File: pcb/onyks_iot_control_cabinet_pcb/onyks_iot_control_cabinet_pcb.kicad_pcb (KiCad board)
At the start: 2 copper layers, 70 x 82 mm, 45 parts, among them J1 Conn_02x05_Odd_Even, J2 Conn_01x06_Pin, J3 Screw_Terminal_01x02, J4 Jack-DC, J5 Conn_01x03_Pin, J6 Screw_Terminal_01x02, J7 Conn_01x02_Socket, J8 Conn_02x09_Odd_Even, J9 Conn_01x06_Socket, Q1 NPN, Q2 NPN, Q3 PMV100ENEAR, Q4 PMV100ENEAR, SW1 SW_Push, SW2 SW_Push, SW3 SW_Push, U1 ESP32-WROOM-32D, U2 LMR51430XDDCR

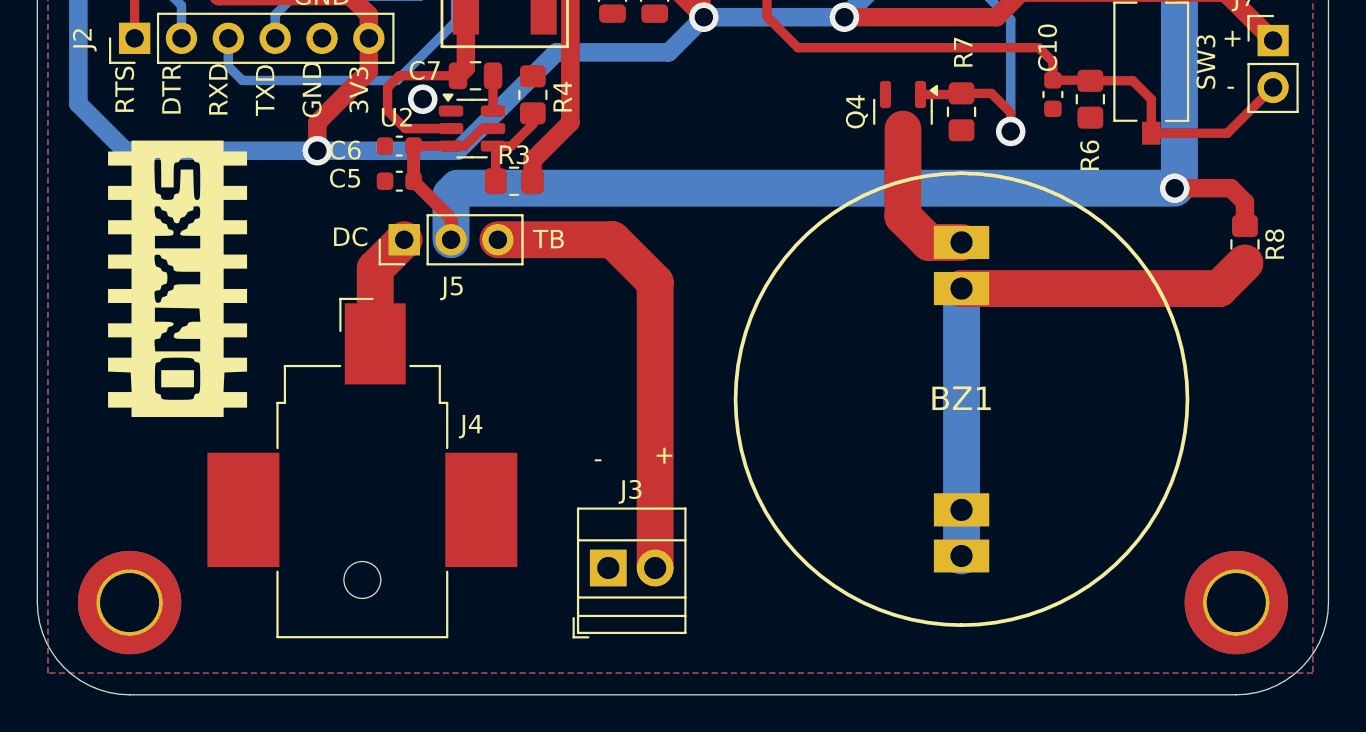
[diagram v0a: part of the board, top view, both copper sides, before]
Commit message: Update the PCB and schematics; add the potentiometer
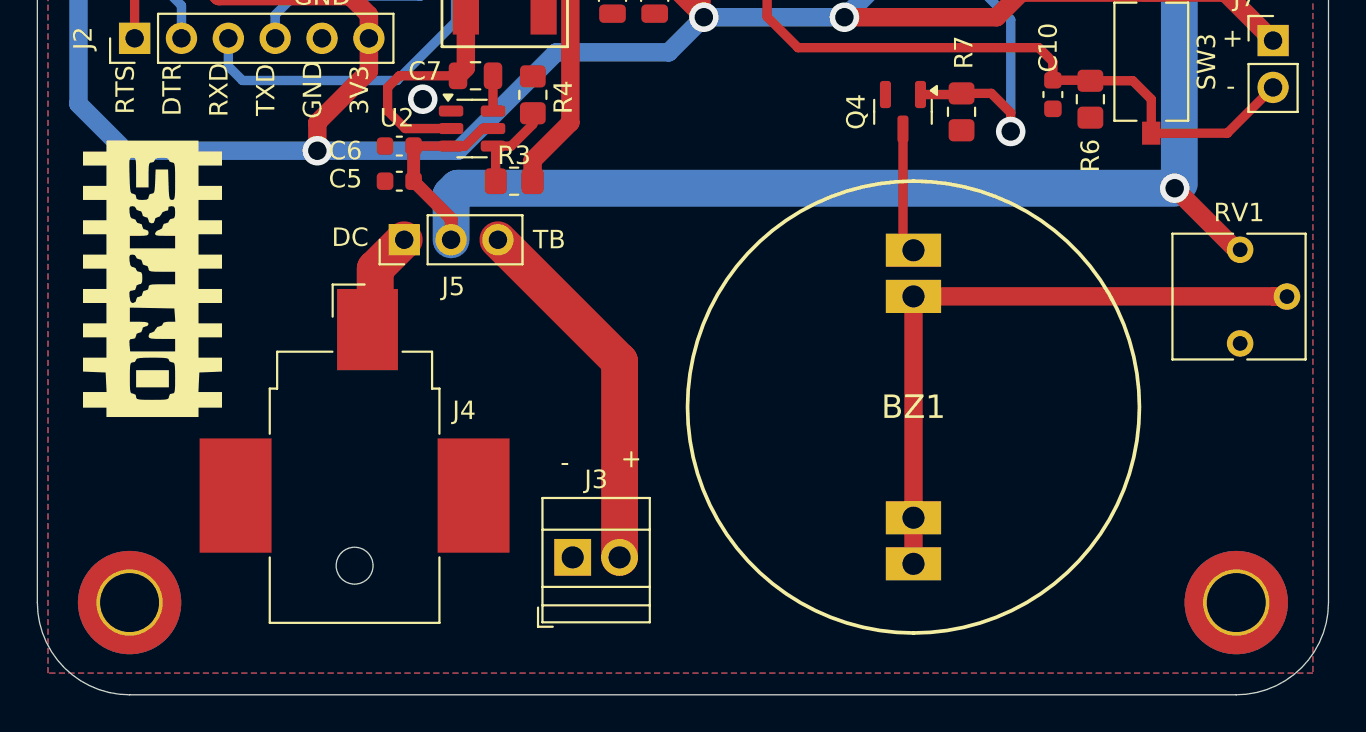
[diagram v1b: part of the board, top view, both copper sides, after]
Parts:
- removed R8: 240, Resistor_SMD:R_0805_2012Metric_Pad1.20x1.40mm_HandSolder
- added RV1: R_Potentiometer, Potentiometer_THT:Potentiometer_Vishay_T73YP_Vertical, F.Cu at (220.2, 106.0)
- R6: value 100k -> 1k
- moved BZ1 2.64 mm to (202.5, 103.4)
- moved J3 2.01 mm to (184.0, 117.5)
- moved G*** 1.36 mm to (161.2, 102.5)
- moved J4 0.88 mm to (172.2, 111.0)
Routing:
- net Net-(J3-Pin_2): track 25.0 -> 20.0 mm
- net Net-(BZ1-+_1): track 30.4 -> 34.8 mm
- net Net-(BZ1--_2): track 8.49 -> 6.81 mm

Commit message: PCB Ressurection
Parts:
- removed BZ1: CPI2416100T, ourFootprints:CPI2416100T
- removed the G*** at (161.2, 102.5)
- removed RV1: R_Potentiometer, Potentiometer_THT:Potentiometer_Vishay_T73YP_Vertical
- added C11: 8.2n/50V, Capacitor_SMD:C_0603_1608Metric, F.Cu at (64.3, 115.2)
- added C12: 10u/10V, Capacitor_SMD:C_0603_1608Metric, F.Cu at (64.3, 117.8)
- added C13: 100n/50V, Capacitor_SMD:C_0603_1608Metric, F.Cu at (64.3, 120.3)
- added C14: 47u/16V, Capacitor_SMD:C_0603_1608Metric, F.Cu at (64.3, 122.8)
- added C15: 47u/16V, Capacitor_SMD:C_0603_1608Metric, F.Cu at (64.3, 125.3)
- added C16: 0.1u/50V, Capacitor_SMD:C_0603_1608Metric, F.Cu at (102.8, 125.7)
- added D3: S5J, Diode_SMD:D_SMC, F.Cu at (90.8, 121.2)
- added G***: LOGO, footprints:LOGO, F.Cu at (208.1, 48.1)
- added IC1: TPS54231DR, footprints:SOIC127P600X175-8N, F.Cu at (52.7, 125.6)
- added J10: Conn_01x05_Pin, Connector_PinHeader_2.54mm:PinHeader_1x05_P2.54mm_Vertical, F.Cu at (107.8, 37.4)
- added J11: Conn_01x06_Socket, Connector_PinHeader_2.54mm:PinHeader_1x06_P2.54mm_Vertical, F.Cu at (103.2, 37.4)
- added LS1: LD-BZPG-2412, footprints:LDBZPG2412, F.Cu at (211.0, 101.8)
- added Q5: PMV100ENEAR, Package_TO_SOT_SMD:SOT-23, F.Cu at (108.0, 52.3)
- added Q6: PMV100ENEAR, Package_TO_SOT_SMD:SOT-23, F.Cu at (108.0, 56.9)
- added R10: 2k/5%, Resistor_SMD:R_0805_2012Metric_Pad1.20x1.40mm_HandSolder, F.Cu at (102.6, 97.6)
- added R11: 3k/5%, Resistor_SMD:R_0805_2012Metric_Pad1.20x1.40mm_HandSolder, F.Cu at (102.6, 100.5)
- added R12: 100k/5%, Resistor_SMD:R_0805_2012Metric_Pad1.20x1.40mm_HandSolder, F.Cu at (102.6, 103.5)
- added R13: 10k/5%, Resistor_SMD:R_0805_2012Metric_Pad1.20x1.40mm_HandSolder, F.Cu at (112.5, 36.6)
- added R14: 10k/5%, Resistor_SMD:R_0805_2012Metric_Pad1.20x1.40mm_HandSolder, F.Cu at (112.5, 39.6)
- added R15: 10k/5%, Resistor_SMD:R_0805_2012Metric_Pad1.20x1.40mm_HandSolder, F.Cu at (112.5, 42.5)
- added R16: 10k/5%, Resistor_SMD:R_0805_2012Metric_Pad1.20x1.40mm_HandSolder, F.Cu at (112.5, 45.5)
- added R8: 100k/5%, Resistor_SMD:R_0805_2012Metric_Pad1.20x1.40mm_HandSolder, F.Cu at (102.6, 91.7)
- added R9: 1k/5%, Resistor_SMD:R_0805_2012Metric_Pad1.20x1.40mm_HandSolder, F.Cu at (102.6, 94.6)
- C10: value 0.1u/50V -> 1n/50V
- C5: value 2.2u/50V -> 4.7u/50V
- C6: value 100n/50V -> 4.7u/50V
- C7: value 100n/50V -> 4.7u/50V; footprint Capacitor_SMD:C_0805_2012Metric -> Capacitor_SMD:C_0603_1608Metric
- C8: value 47n/10V -> 10u/10V; footprint Capacitor_SMD:C_0805_2012Metric -> Capacitor_SMD:C_0603_1608Metric
- C9: value 47n/10V -> 10p/50V; footprint Capacitor_SMD:C_0805_2012Metric -> Capacitor_SMD:C_0603_1608Metric
- D2: value S5J -> B360
- J3, J6: footprint TerminalBlock:TerminalBlock_Xinya_XY308-2.54-2P_1x02_P2.54mm_Horizontal -> TerminalBlock:TerminalBlock_Altech_AK300-2_P5.00mm
- J4: value Jack-DC -> Barrel_Jack_Switch; footprint Connector_BarrelJack:BarrelJack_CUI_PJ-036AH-SMT_Horizontal -> Connector_BarrelJack:BarrelJack_CLIFF_FC681465S_SMT_Horizontal
- J8: value Conn_02x09_Odd_Even -> Conn_01x03_Pin; footprint Connector_PinHeader_2.54mm:PinHeader_2x09_P2.54mm_Vertical -> Connector_PinHeader_2.54mm:PinHeader_1x03_P2.54mm_Vertical
- J9: value Conn_01x06_Socket -> Conn_02x09_Odd_Even; footprint Connector_PinHeader_2.54mm:PinHeader_1x06_P2.54mm_Vertical -> Connector_PinHeader_2.54mm:PinHeader_2x09_P2.54mm_Vertical
- L1: value XAL6060-562MEC_COC -> 15u; footprint ourFootprints:XAL6060-562MEC_COC -> Inductor_SMD:L_12x12mm_H4.5mm
- Q1, Q2: value NPN -> BC847B
- R1, R2: value 10k -> 10k/5%
- R3: value 100k -> 10k/1%
- R4: value 22.1k -> 1M/1%
- R5: value 100k -> 45.3k/1%
- R6: value 1k -> 10.2k/1%
- R7: value 100k -> 1.96k/1%
- U2: value LMR51430XDDCR -> LM1117MP-3.3; footprint Package_TO_SOT_SMD:SOT-23-6 -> Package_TO_SOT_SMD:SOT-223-3_TabPin2
- moved D2 159.9 mm to (53.9, 110.1), turned to 0 degrees
- moved C10 153.8 mm to (60.3, 127.8), turned to 0 degrees
- moved R6 146.8 mm to (68.7, 124.3), turned to 0 degrees
- moved R7 140.5 mm to (68.7, 127.3), turned to 0 degrees
- moved R5 138.0 mm to (68.7, 121.4), turned to 0 degrees
- moved SW1 134.3 mm to (40.4, 80.3), turned to 0 degrees
- moved C9 133.7 mm to (60.3, 125.3), turned to 0 degrees
- moved C4 133.1 mm to (47.7, 86.5), turned to 0 degrees
- moved C8 130.8 mm to (60.3, 122.8), turned to 0 degrees
- moved C3 130.7 mm to (47.7, 84.0), turned to 0 degrees
- moved SW3 130.2 mm to (90.6, 127.7), turned to 0 degrees
- moved J8 129.8 mm to (98.5, 119.6)
- moved D1 129.2 mm to (58.9, 81.0)
- moved SW2 127.7 mm to (40.4, 85.6), turned to 0 degrees
- moved U2 127.4 mm to (53.4, 118.2)
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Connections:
- C10 pad 1: /MCU/GPIO_19 -> Net-(C10-Pad1)
- C5 pad 1: +12V -> +24V
- C6 pad 1: +12V -> +24V
- C7 pad 1: Net-(U2-CB) -> +24V
- C7 pad 2: Net-(U2-SW) -> GND
- C8 pad 1: +3.3V -> +5V
- C9 pad 1: +3.3V -> Net-(IC1-COMP)
- D2 pad 1: +12V -> Net-(D2-K)
- D2 pad 2: Net-(D2-A) -> GND
- J5 pad 2: +12V -> +24V
- J6 pad 1: +12V -> +24V
- J6 pad 2: Net-(D2-A) -> Net-(D3-A)
- J7 pad 2: /MCU/GPIO_19 -> /MCU/GPIO_18
- J8 pad 1: /MCU/GPIO_2 -> +24V
- J8 pad 2: GND -> Net-(J8-Pin_2)
- J8 pad 3: /MCU/GPIO_5 -> Net-(J8-Pin_3)
- J9 pad 1: /MCU/GPIO_23 -> /MCU/GPIO_16
- J9 pad 2: /MCU/GPIO_25 -> GND
- J9 pad 3: /MCU/GPIO_26 -> /MCU/GPIO_16
- J9 pad 5: /MCU/GPIO_27 -> /MCU/GPIO_33
- J9 pad 6: +3.3V -> GND
- L1 pad 1: Net-(U2-SW) -> Net-(D2-K)
- L1 pad 2: +3.3V -> +5V
- Q3 pad 1: /MCU/GPIO_18 -> /MCU/GPIO_17
- Q3 pad 3: Net-(D2-A) -> Net-(D3-A)
- Q4 pad 1: /MCU/GPIO_4 -> /MCU/GPIO_19
- R3 pad 1: +3.3V -> +24V
- R3 pad 2: Net-(U2-FB) -> Net-(IC1-EN)
- R4 pad 1: Net-(U2-FB) -> Net-(IC1-EN)
- R5 pad 1: /MCU/GPIO_18 -> Net-(IC1-COMP)
- R5 pad 2: GND -> Net-(C10-Pad1)
- R6 pad 1: /MCU/GPIO_19 -> +5V
- R6 pad 2: GND -> Net-(IC1-VSENSE)
- R7 pad 1: /MCU/GPIO_4 -> Net-(IC1-VSENSE)
- SW3 pad 2: /MCU/GPIO_19 -> /MCU/GPIO_18
- U1 pad 24: /MCU/GPIO_2 -> /MCU/GPIO_16
- U1 pad 26: /MCU/GPIO_4 -> /MCU/GPIO_16
- U1 pad 29: /MCU/GPIO_5 -> /MCU/GPIO_33
- U2 pad 2: Net-(U2-SW) -> +3.3V
- U2 pad 3: +12V -> +5V
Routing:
- net +3.3V: track 227.2 -> 0.00 mm, vias 6 -> 0
- net /MCU/GPIO_25: track 82.2 -> 0.00 mm, vias 1 -> 0
- net /MCU/GPIO_26: track 80.1 -> 0.00 mm, vias 1 -> 0
- net +12V: track 78.6 -> 0.00 mm, vias 1 -> 0
- net /MCU/RXD: track 76.4 -> 0.00 mm, vias 1 -> 0
- net /MCU/GPIO_27: track 75.3 -> 0.00 mm, vias 1 -> 0
- net /MCU/TXD: track 71.1 -> 0.00 mm, vias 1 -> 0
- net /MCU/GPIO_19: track 65.9 -> 0.00 mm, vias 2 -> 0
- net /MCU/MCU_BOOT: track 60.8 -> 0.00 mm, vias 2 -> 0
- net /MCU/GPIO_34: track 59.9 -> 0.00 mm, vias 2 -> 0
- net /MCU/GPIO_33: track 59.7 -> 0.00 mm, vias 3 -> 0
- net /MCU/GPIO_35: track 59.7 -> 0.00 mm, vias 2 -> 0
- net /MCU/GPIO_4: track 48.5 -> 0.00 mm, vias 4 -> 0
- net /MCU/RTS: track 45.2 -> 0.00 mm
- net /MCU/DTR: track 39.2 -> 0.00 mm, vias 1 -> 0
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- removed copper zone on B.Cu, net GND
- removed copper zone on F.Cu, net GND
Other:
- board text removed: "+"
- board text removed: "-"
- board text removed: "16"
- board text removed: "17"
- board text removed: "2"
- board text removed: "21"
- board text removed: "22"
- board text removed: "33"
- board text removed: "34"
- board text removed: "35"
- board text removed: "3V3"
- board text removed: "5"
- board text removed: "DC"
- board text removed: "DTR"
- board text removed: "GND"
- board text removed: "IRQ"
- board text removed: "MISO"
- board text removed: "MOSI"
- board text removed: "MTCK"
- board text removed: "MTDI"
- board text removed: "MTDO"
- board text removed: "MTMS"
- board text removed: "RST"
- board text removed: "RTS"
- board text removed: "RXD"
- board text removed: "TB"
- board text removed: "TXD"

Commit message: PCB Update
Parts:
- moved SW1 137.2 mm to (176.4, 62.6), turned to -90 degrees
- moved C3 136.3 mm to (178.6, 46.1), turned to 90 degrees
- moved C4 134.3 mm to (175.8, 46.1), turned to 90 degrees
- moved U2 133.2 mm to (184.7, 95.6), turned to -90 degrees
- moved SW2 132.1 mm to (170.4, 62.6), turned to -90 degrees
- moved C1 127.9 mm to (173.9, 58.3), turned to 180 degrees
- moved Q2 127.0 mm to (174.4, 49.8), turned to 90 degrees
- moved D1 125.7 mm to (183.7, 66.7)
- moved Q1 124.6 mm to (174.4, 55.2), turned to -90 degrees
- moved C12 124.2 mm to (185.4, 89.9)
- moved C2 122.4 mm to (167.9, 58.3), turned to 180 degrees
- moved C8 121.7 mm to (179.5, 97.8), turned to -90 degrees
- moved J11 118.1 mm to (220.0, 55.4)
- moved J10 117.6 mm to (220.0, 72.9)
- moved C10 117.0 mm to (174.1, 100.6), turned to 90 degrees
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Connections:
- J9 pad 1: /MCU/GPIO_16 -> /MCU/GPIO_2
- J9 pad 3: /MCU/GPIO_16 -> /MCU/GPIO_4
- J9 pad 5: /MCU/GPIO_33 -> /MCU/GPIO_5
- U1 pad 24: /MCU/GPIO_16 -> /MCU/GPIO_2
- U1 pad 26: /MCU/GPIO_16 -> /MCU/GPIO_4
- U1 pad 29: /MCU/GPIO_33 -> /MCU/GPIO_5
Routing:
- net /MCU/GPIO_27: track 0.00 -> 64.2 mm, vias 0 -> 1
- net /MCU/GPIO_26: track 0.00 -> 63.5 mm, vias 0 -> 1
- net /MCU/GPIO_25: track 0.00 -> 58.6 mm, vias 0 -> 1
- net +24V: track 0.00 -> 41.6 mm
- net +3.3V: track 0.00 -> 41.5 mm
- net /MCU/GPIO_22: track 0.00 -> 33.2 mm
- net Net-(J3-Pin_2): track 0.00 -> 27.6 mm
- net /MCU/GPIO_23: track 0.00 -> 25.9 mm
- net /MCU/MCU_RESET: track 0.00 -> 24.2 mm
- net /MCU/GPIO_21: track 0.00 -> 22.8 mm
- net Net-(J8-Pin_2): track 0.00 -> 22.6 mm
- net Net-(LS1--): track 0.00 -> 21.5 mm
- net GND: track 0.00 -> 21.1 mm, vias 0 -> 7
- net Net-(J5-Pin_1): track 0.00 -> 19.0 mm
- net Net-(IC1-COMP): track 0.00 -> 16.9 mm, vias 0 -> 2
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- added copper zone on B.Cu, net +24V
- added copper zone on F.Cu, net +24V
- added copper zone on F.Cu, net +5V
- added copper zone on B.Cu, net GND
- added copper zone on F.Cu, net GND
- added copper zone on F.Cu, net Net-(D2-K)
- added copper zone on F.Cu, net Net-(D3-A)

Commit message: Updated PCB 2
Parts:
- moved J7 83.2 mm to (200.4, 70.6), turned to 90 degrees
- moved SW3 80.9 mm to (201.4, 66.2), turned to 0 degrees
- moved C16 80.1 mm to (204.7, 74.3), turned to -90 degrees
- moved R9 69.0 mm to (202.0, 73.8), turned to 180 degrees
- moved SW1 15.2 mm to (161.5, 59.5), turned to 180 degrees
- moved SW2 12.4 mm to (161.5, 54.0), turned to 180 degrees
- moved D1 9.64 mm to (191.3, 72.7), turned to 180 degrees
- moved C1 6.60 mm to (167.5, 56.6), turned to 90 degrees
- moved C2 2.68 mm to (165.8, 56.7), turned to -90 degrees
- moved Q1 2.64 mm to (172.8, 53.0)
- moved Q2 2.64 mm to (172.8, 47.6)
- moved R1 2.64 mm to (167.8, 48.1)
- moved R2 2.64 mm to (167.8, 52.8)
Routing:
- net +3.3V: track 41.5 -> 151.9 mm, vias 0 -> 2
- net /MCU/GPIO_19: track 3.41 -> 82.5 mm, vias 0 -> 2
- net /MCU/MCU_BOOT: track 7.42 -> 77.6 mm, vias 0 -> 2
- net /MCU/RXD: track 0.00 -> 59.1 mm, vias 0 -> 1
- net /MCU/TXD: track 0.00 -> 57.6 mm, vias 0 -> 1
- net /MCU/RTS: track 5.43 -> 55.9 mm, vias 0 -> 1
- net /MCU/GPIO_22: track 33.2 -> 80.5 mm, vias 0 -> 2
- net /MCU/GPIO_17: track 1.90 -> 45.7 mm, vias 0 -> 5
- net /MCU/GPIO_34: track 0.00 -> 39.2 mm, vias 0 -> 1
- net /MCU/GPIO_35: track 0.00 -> 37.6 mm, vias 0 -> 1
- net /MCU/GPIO_21: track 22.8 -> 60.1 mm, vias 0 -> 4
- net /MCU/DTR: track 6.04 -> 41.5 mm, vias 0 -> 1
- net /MCU/GPIO_18: track 0.00 -> 33.0 mm, vias 0 -> 2
- net /MCU/GPIO_33: track 0.00 -> 32.7 mm, vias 0 -> 1
- net /MCU/GPIO_32: track 0.00 -> 32.6 mm, vias 0 -> 2
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- added copper zone on B.Cu, net +3.3V
- added copper zone on B.Cu, net +5V

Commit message: PCB 3.3V fix
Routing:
- net /MCU/RXD: track 59.1 -> 46.6 mm
- net +3.3V: track 151.9 -> 142.3 mm
- net /MCU/TXD: track 57.6 -> 60.0 mm
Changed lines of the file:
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@@
 	)
 	(segment
-		(start 209.7786 77.6986)
-		(end 205.74 77.6986)
-		(width 1)
-		(layer "B.Cu")
-		(net 1)
-	)
-	(segment
-		(start 212.7758 77.6986)
-		(end 209.7786 77.6986)
-		(width 1)
-		(layer "B.Cu")
-		(net 1)
-	)
-	(segment
 		(start 178.6128 79.0956)
 		(end 179.5272 80.01)
@@
 	)
 	(segment
-		(start 214.6046 75.8698)
-		(end 212.7758 77.6986)
-		(width 1)
-		(layer "B.Cu")
-		(net 1)
-	)
-	(segment
 		(start 178.6128 72.644)
 		(end 178.6128 79.0956)
@@
 	)
 	(segment
-		(start 195.4784 86.5124)
-		(end 195.4784 74.05432)
-		(width 0.508)
-		(layer "B.Cu")
-		(net 33)
-	)
-	(segment
 		(start 185.293 83.82)
 		(end 185.293 85.022081)
@@
 	)
 	(segment
-		(start 194.6402 74.7014)
-		(end 194.6402 86.0806)
+		(start 194.6402 80.255349)
+		(end 194.6402 74.7014)
 		(width 0.508)
 		(layer "B.Cu")
@@
 	)
 	(segment
+		(start 189.138 82.515)
+		(end 192.380549 82.515)
+		(width 0.508)
+		(layer "B.Cu")
+		(net 34)
+	)
+	(segment
+		(start 192.380549 82.515)
+		(end 194.6402 80.255349)
+		(width 0.508)
+		(layer "B.Cu")
+		(net 34)
+	)
+	(segment
 		(start 194.1068 50.3682)
 		(end 192.3542 52.1208)
@@
 	)
 	(segment
+		(start 187.833 83.82)
+		(end 189.138 82.515)
+		(width 0.508)
+		(layer "B.Cu")
+		(net 34)
+	)
+	(segment
 		(start 172.847 56.0832)
 		(end 172.847 54.1455)
@@
 			)
 		)
+	)
+	(zone
+		(net 1)
+		(net_name "+3.3V")
+		(layer "B.Cu")
+		(hatch edge 0.5)
+		(priority 10)
+		(connect_pads
+			(clearance 0)
+		)
+		(min_thickness 0.25)
+		(filled_areas_thickness no)
+		(fill yes
+			(thermal_gap 0.5)
+			(thermal_bridge_width 0.5)
+		)
+		(polygon
+			(pts
+				(xy 212.9536 74.5744) (xy 216.4334 74.5744) (xy 216.4334 77.2922) (xy 214.7062 79.0194) (xy 204.9526 79.0194)
+				(xy 204.9526 76.2) (xy 212.9536 76.2)
+			)
+		)

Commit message: PCB Update 3
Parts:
- moved C1 0.28 mm to (167.8, 56.6)
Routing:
- net /MCU/RXD: track 46.6 -> 58.2 mm
- net +3.3V: track 142.3 -> 135.0 mm
- net /MCU/TXD: track 60.0 -> 56.4 mm

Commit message: PCB descriptions
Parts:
- moved Q3 4.15 mm to (175.6, 78.7)
- moved R8 4.15 mm to (178.4, 78.6)
- moved D1 3.13 mm to (191.4, 69.6)
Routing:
- net /MCU/GPIO_17: track 45.7 -> 38.5 mm, vias 5 -> 4
- net /MCU/GPIO_32: track 32.6 -> 28.3 mm
- net +3.3V: track 135.0 -> 133.4 mm
- net /MCU/MTDO: track 16.6 -> 17.2 mm
- net /MCU/MTDI: track 17.5 -> 17.0 mm
- net GND: vias 16 -> 17
- net /MCU/MCU_RESET: vias 1 -> 0
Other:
- board text added: "+"
- board text added: "-"
- board text added: "125kHz"
- board text added: "13MHz"
- board text added: "16"
- board text added: "2"
- board text added: "3.3V"
- board text added: "33"
- board text added: "34"
- board text added: "35"
- board text added: "3V3"
- board text added: "5"
- board text added: "5V"
- board text added: "BOOT"
- board text added: "DIV"
- board text added: "DTR"
- board text added: "GND"
- board text added: "IRQ"
- board text added: "JACK"
- board text added: "LOCK+"
- board text added: "LOCK-"
- board text added: "MISO"
- board text added: "MOSI"
- board text added: "MTCK"
- board text added: "MTDI"
- board text added: "MTDO"
- board text added: "MTMS"
- board text added: "RESET"
- board text added: "RST"
- board text added: "RTS"
- board text added: "RX"
- board text added: "RXD"
- board text added: "TB"
- board text added: "TX"
- board text added: "TXD"
- board text added: "VCC"
